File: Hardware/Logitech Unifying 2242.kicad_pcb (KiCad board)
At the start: 2 copper layers, 22 x 42 mm, 13 parts, among them J1 Bus_M.2_Socket_B, U1 TPS613222ADBV

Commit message: Add PCB text
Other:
- board text added: "${TITLE} Revision ${REVISION} ${ISSUE_DATE}"
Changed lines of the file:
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@@
     )
+  )
+  (gr_text "${TITLE}\nRevision ${REVISION}\n${ISSUE_DATE}" (at 138.6 113.1) (layer "B.SilkS")
+    (effects (font (size 1 1) (thickness 0.2)) (justify mirror))
   )
   (segment (start 144.1445 112.444) (end 144.1445 110.412) (width 0.25) (layer "F.Cu") (net 1))

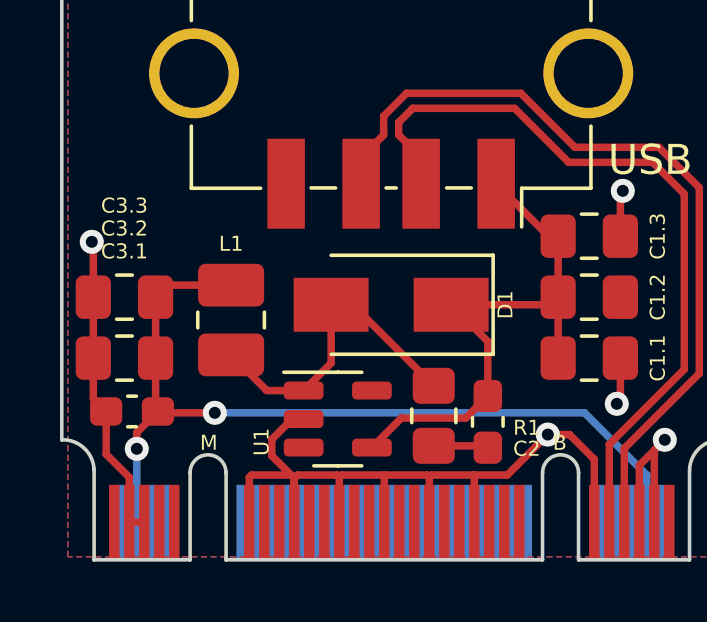
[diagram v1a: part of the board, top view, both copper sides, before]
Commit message: Reduce fill clearance and add more GND vias
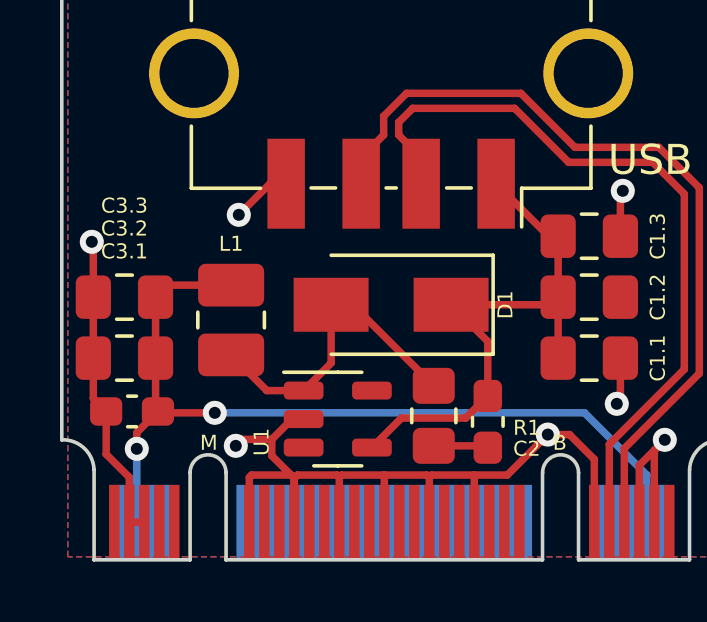
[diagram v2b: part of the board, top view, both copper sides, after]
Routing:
- net GND: track 47.8 -> 51.1 mm, vias 5 -> 7
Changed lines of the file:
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@@
   (segment (start 146.2195 110.412) (end 146.2195 108.9805) (width 0.25) (layer "F.Cu") (net 2))
   (segment (start 135.35 118.47975) (end 135.35 119.95) (width 0.25) (layer "F.Cu") (net 2))
+  (segment (start 134.6 117.186249) (end 133.613751 117.186249) (width 0.25) (layer "F.Cu") (net 2))
   (segment (start 128.6505 114.476) (end 128.6505 115.825) (width 0.25) (layer "F.Cu") (net 2))
   (segment (start 139.85 118.45) (end 139.925 118.375) (width 0.25) (layer "F.Cu") (net 2))
@@
   (segment (start 146.2195 114.476) (end 146.2195 115.8805) (width 0.25) (layer "F.Cu") (net 2))
   (segment (start 141.35 118.375) (end 142.4495 118.375) (width 0.25) (layer "F.Cu") (net 2))
+  (segment (start 133.613751 117.186249) (end 133.4 117.4) (width 0.25) (layer "F.Cu") (net 2))
   (segment (start 129.85 119.95) (end 129.85 118.45) (width 0.25) (layer "F.Cu") (net 2))
   (segment (start 146.2195 115.8805) (end 146.1 116) (width 0.25) (layer "F.Cu") (net 2))
@@
   (segment (start 128.6505 110.6505) (end 128.6 110.6) (width 0.25) (layer "F.Cu") (net 2))
   (segment (start 136.85 118.45) (end 136.775 118.375) (width 0.25) (layer "F.Cu") (net 2))
+  (segment (start 135.078 108.664) (end 134.536 108.664) (width 0.25) (layer "F.Cu") (net 2))
   (segment (start 128.6505 114.476) (end 128.6505 112.444) (width 0.25) (layer "F.Cu") (net 2))
   (segment (start 135.24525 118.375) (end 135.35 118.47975) (width 0.25) (layer "F.Cu") (net 2))
@@
   (segment (start 136.775 118.375) (end 135.454751 118.375) (width 0.25) (layer "F.Cu") (net 2))
   (segment (start 136.85 118.45) (end 136.925 118.375) (width 0.25) (layer "F.Cu") (net 2))
+  (segment (start 134.536 108.664) (end 133.5 109.7) (width 0.25) (layer "F.Cu") (net 2))
   (segment (start 128.6505 115.825) (end 129.0795 116.254) (width 0.25) (layer "F.Cu") (net 2))
   (segment (start 129.85 118.45) (end 129.0795 117.6795) (width 0.25) (layer "F.Cu") (net 2))
@@
   (segment (start 135.454751 118.375) (end 135.35 118.479751) (width 0.25) (layer "F.Cu") (net 2))
   (via (at 128.6 110.6) (size 0.8) (drill 0.4) (layers "F.Cu" "B.Cu") (net 2))
+  (via (at 133.4 117.4) (size 0.8) (drill 0.4) (layers "F.Cu" "B.Cu") (net 2))
   (via (at 146.1 116) (size 0.8) (drill 0.4) (layers "F.Cu" "B.Cu") (net 2))
   (via (at 146.3 108.9) (size 0.8) (drill 0.4) (layers "F.Cu" "B.Cu") (net 2))
   (via (at 143.8 117.0245) (size 0.8) (drill 0.4) (layers "F.Cu" "B.Cu") (net 2))
   (via (at 147.7 117.2) (size 0.8) (drill 0.4) (layers "F.Cu" "B.Cu") (net 2))
+  (via (at 133.5 109.7) (size 0.8) (drill 0.4) (layers "F.Cu" "B.Cu") (net 2))
   (segment (start 141.7375 117.4) (end 141.8 117.4625) (width 0.25) (layer "F.Cu") (net 3))
   (segment (start 140 117.4) (end 141.7375 117.4) (width 0.25) (layer "F.Cu") (net 3))
@@
   (segment (start 138.828 106.619638) (end 139.297638 106.15) (width 0.25) (layer "F.Cu") (net 10))
   (zone (net 2) (net_name "GND") (layers F&B.Cu) (hatch edge 0.508)
-    (connect_pads (clearance 0.508))
+    (connect_pads (clearance 0.25))
     (min_thickness 0.254) (filled_areas_thickness no)
     (fill yes (thermal_gap 0.508) (thermal_bridge_width 0.508))
